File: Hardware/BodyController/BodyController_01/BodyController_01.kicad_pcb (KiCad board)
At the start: 4 copper layers, 155 x 106 mm, 402 parts, among them J1 7796, J10 Conn_01x01, J11 Conn_01x01, J12 Conn_01x01, J13 Conn_01x01, J2 Conn_01x14, J3 Conn_02x10_Top_Bottom, J4 Conn_02x10_Top_Bottom, J5 7796, J6 7796, J7 CONN_01X06, J8 USB_OTG, J9 Conn_01x01, Q1 NX1029X,115, Q10 NX1029X,115, Q12 BUK9Y3R0-40E,115, Q13 BUK9Y3R0-40E,115, Q16 2N7002, Q17 Q_PMOS_GSD, Q2 NX1029X,115, Q3 2N7002, Q4 SQJ423EP-T1_GE3, Q6 NX1029X,115, Q7 NX1029X,115, Q8 2N7002, Q9 2N7002, SW1 PTS645SM43SMTR92 LFS, U1 PIC33EPxxxMU810, U10 LM2904AVQDRQ1, U11 BTS50202EKAXUMA2, U12 BTS50202EKAXUMA2, U13 BTS50202EKAXUMA2, U14 OPA320-Q1, U15 BTS716G, U16 MCP2562-H/SN, U17 TPS70950QDBVRQ1, U18 TPS70933QDBVRQ1, U19 TPS70933QDBVRQ1, U2 LM2903QDRQ1, U20 LMR140x0, U21 LM2903QDRQ1, U22 DRV8872DDARQ1, U23 tps25940-q1, U25 UCC27511A-Q1, U27 INA21x, U29 FT230X, U3 INA21x, U4 BTS716G, U5 BTS500801TMAATMA1, U6 BTS500801TMAATMA1, U7 BTS50202EKAXUMA2, U8 BTS50202EKAXUMA2, U9 BTS50202EKAXUMA2, Y1 8MHz

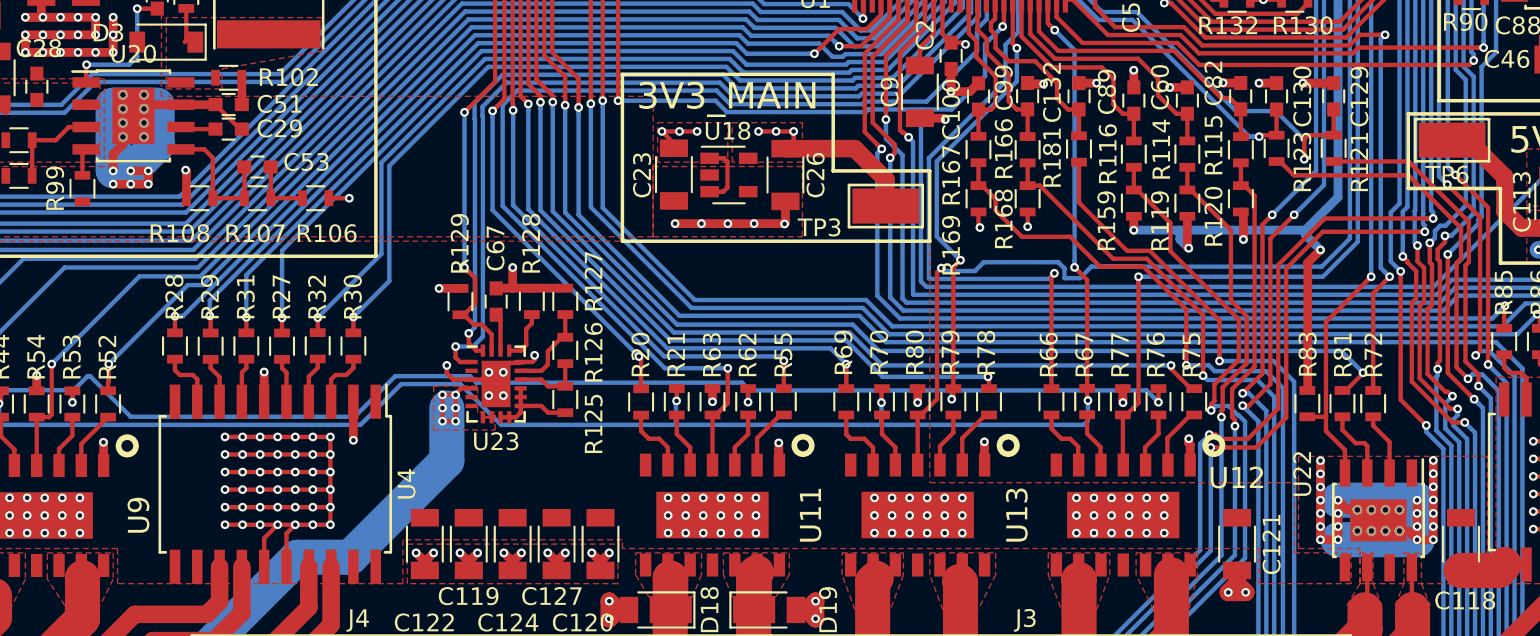
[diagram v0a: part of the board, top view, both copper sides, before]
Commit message: added BOM scripts
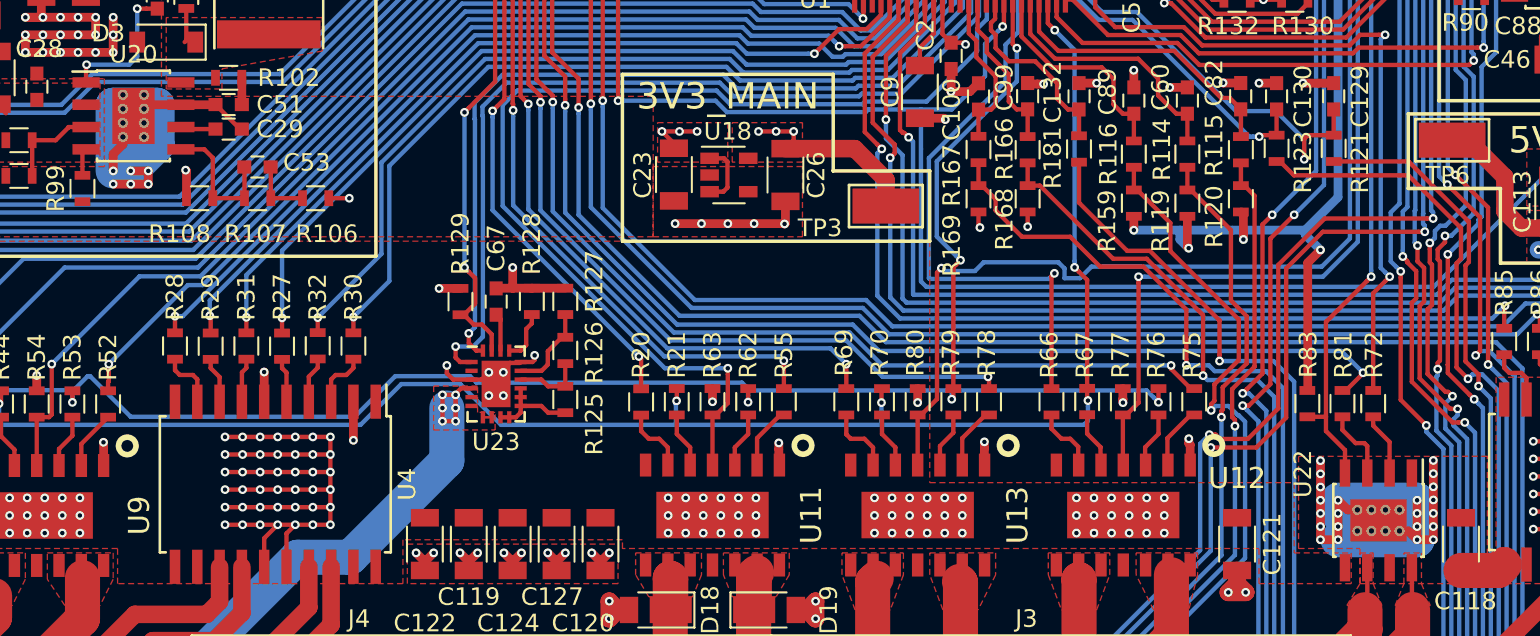
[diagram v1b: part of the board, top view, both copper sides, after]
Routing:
- net GND: track 980.4 -> 986.4 mm
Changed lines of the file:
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@@
     (thickness 1.6)
     (drawings 92)
-    (tracks 5516)
+    (tracks 5519)
     (zones 0)
     (modules 402)
@@
   (segment (start 112.5 127.752916) (end 112.499692 127.752608) (width 0.25) (layer F.Cu) (net 202))
   (segment (start 112.5 128.5) (end 112.5 127.752916) (width 0.25) (layer F.Cu) (net 202))
-  (segment (start 163.85 135.5) (end 166.25 135.5) (width 2) (layer In1.Cu) (net 209))
+  (segment (start 94.755 112.266) (end 94.355 112.266) (width 2) (layer B.Cu) (net 209))
+  (segment (start 94.355 112.266) (end 93.555 113.066) (width 2) (layer B.Cu) (net 209))
+  (segment (start 162.75 134.5) (end 167.25 134.5) (width 2) (layer B.Cu) (net 209))
   (segment (start 162.75 133.75) (end 167.25 133.75) (width 2) (layer B.Cu) (net 209))
+  (segment (start 163.85 135.5) (end 166.25 135.5) (width 2) (layer In1.Cu) (net 209))
   (segment (start 162.75 136) (end 167.25 136) (width 2) (layer B.Cu) (net 209))
   (segment (start 94.755 110.666) (end 94.755 113.066) (width 2) (layer In1.Cu) (net 209))

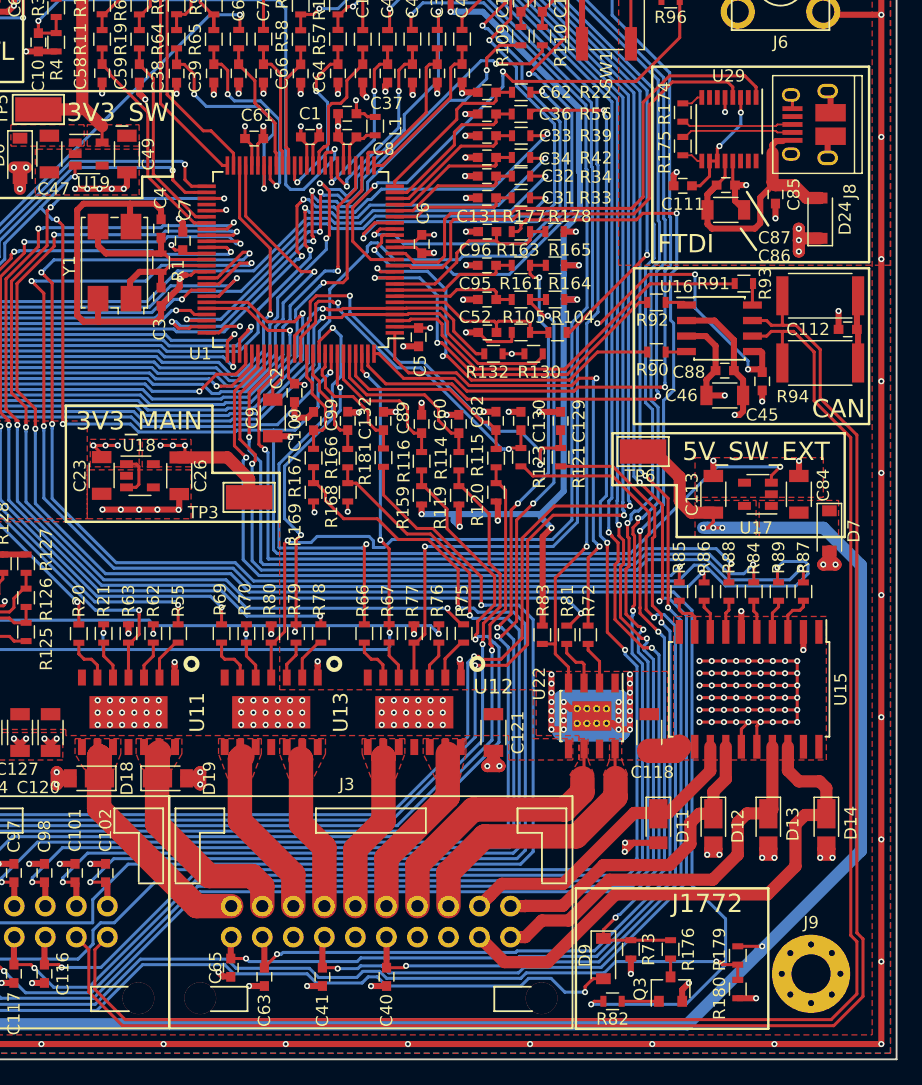
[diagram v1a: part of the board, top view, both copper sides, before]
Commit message: fixed some BOM items, changed USB to vertical mount, CAN traces thicker, J1172 sims
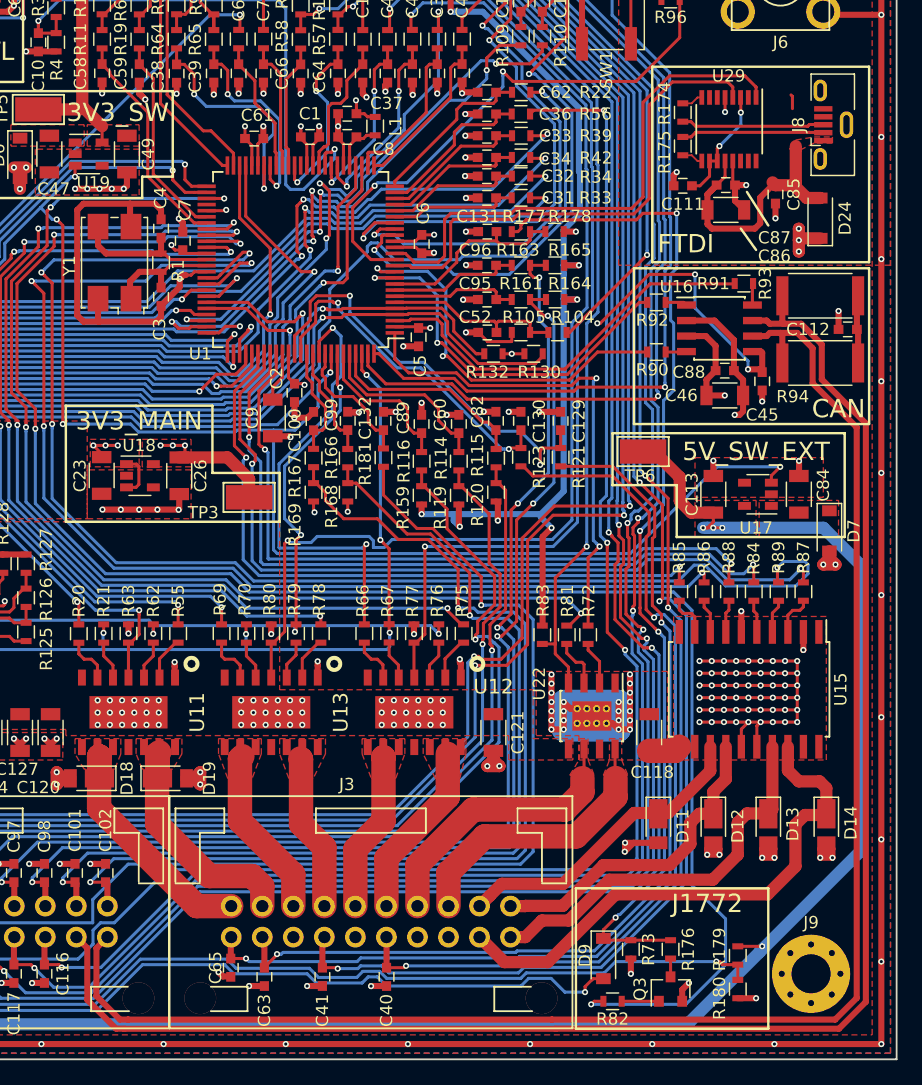
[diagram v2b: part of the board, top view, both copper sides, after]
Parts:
- J8: footprint Connectors:USB_Micro-B_10103594-0001LF -> Connectors_USB:USB_Micro-B_Vertical_Molex-105133-0001
- R176: value R -> 1k3
- R177: value R -> 340k
- R178: value R -> 100k
- R179, R180: value R -> 330R
- R181: value R -> 10k
- R73: value R -> 2k74
- R82: value R -> 100R
- moved J8 1.85 mm to (184.8, 86.5)
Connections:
- net PILOT_IN renamed PILOT
- net PROXIMITY_IN renamed PROXIMITY
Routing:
- net GND: track 986.4 -> 981.5 mm
- net USB_D+: track 9.17 -> 11.9 mm
- net USB_D-: track 9.23 -> 11.9 mm
- net USB_5V: track 24.4 -> 22.6 mm
- net CAN_P: track 133.8 -> 135.3 mm
- net (no net): track 0.00 -> 1.17 mm
- added copper zone on F.Cu, net USB_5V

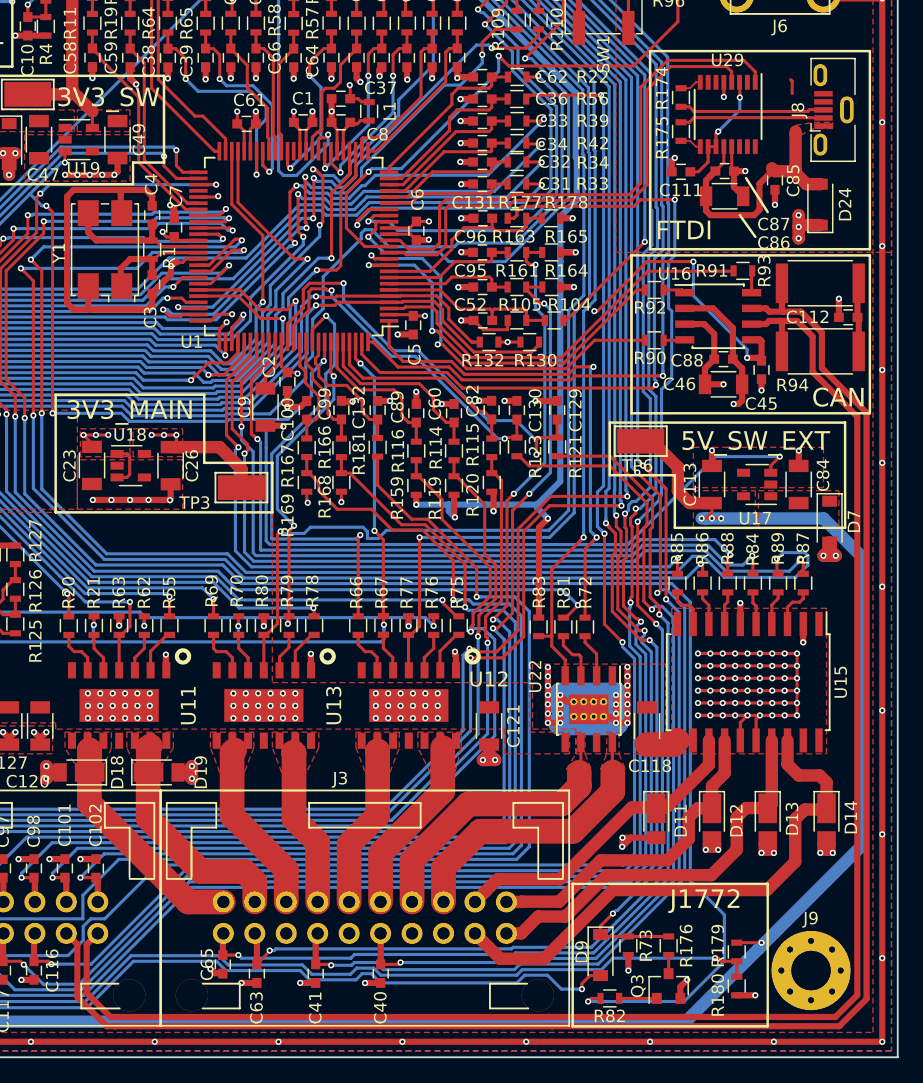
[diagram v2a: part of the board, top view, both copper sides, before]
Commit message: added CAN choke
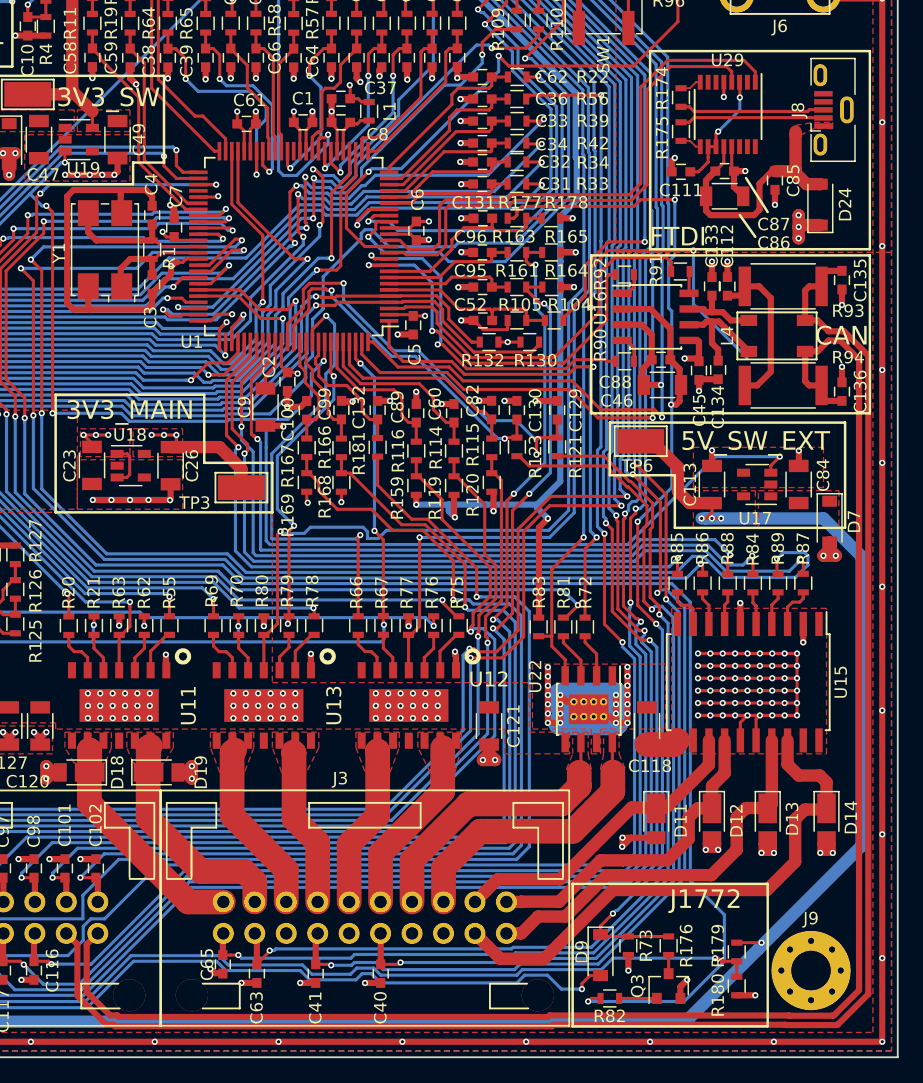
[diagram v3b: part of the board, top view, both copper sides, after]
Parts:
- added C133: 18pF, Capacitors_SMD:C_0603, F.Cu at (175.0, 100.8)
- added C134: 18pF, Capacitors_SMD:C_0603, F.Cu at (175.5, 107.5)
- added C135: 18pF, Capacitors_SMD:C_0603, F.Cu at (185.5, 100.2)
- added C136: 18pF, Capacitors_SMD:C_0603, F.Cu at (185.5, 109.2)
- added L4: EMI_Filter_CommonMode, Footprints:ACT45B, F.Cu at (180.2, 104.8)
- moved C112 10.1 mm to (176.2, 100.8), turned to 90 degrees
- moved C45 5.05 mm to (173.9, 107.5)
- moved C88 5.05 mm to (170.9, 106.7)
- moved R91 5.05 mm to (172.4, 99.5)
- moved U16 5.05 mm to (170.4, 103.2)
- moved C46 4.94 mm to (171.0, 108.7)
- moved R94 4.07 mm to (180.8, 108.8), turned to 180 degrees
- moved R93 3.01 mm to (180.8, 100.8), turned to 0 degrees
- moved R90 2.94 mm to (167.9, 106.8)
- moved R92 2.70 mm to (167.9, 99.8)
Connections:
- U16 pad 6: CAN_N -> /TopLevel/Communication/CAN_FILT_N
- U16 pad 7: CAN_P -> /TopLevel/Communication/CAN_FILT_P
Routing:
- net (no net): track 1.17 -> 22.6 mm, vias 0 -> 2
- net +3V3: track 62.3 -> 43.1 mm, vias 18 -> 16
- net /TopLevel/Communication/CAN_FILT_N: track 0.00 -> 9.30 mm
- net Net-(C112-Pad1): track 5.58 -> 13.0 mm
- net /TopLevel/Communication/CAN_FILT_P: track 0.00 -> 6.54 mm
- net GND: track 981.5 -> 986.5 mm, vias 312 -> 315
- net BATT_EN: track 178.0 -> 182.4 mm
- net DCDC_EN: track 146.5 -> 149.8 mm
- net CAN_RX: track 31.9 -> 28.9 mm
- net CAN_SLEEP: track 33.0 -> 31.1 mm
- net +12P: track 220.3 -> 221.9 mm
- net Net-(R92-Pad1): track 1.79 -> 2.47 mm
- net CAN_P: track 135.3 -> 135.9 mm
- net RADIATOR_INPUT_TEMP_OUT: track 151.6 -> 152.1 mm
- net DAC_OUT_1: track 182.4 -> 181.8 mm
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
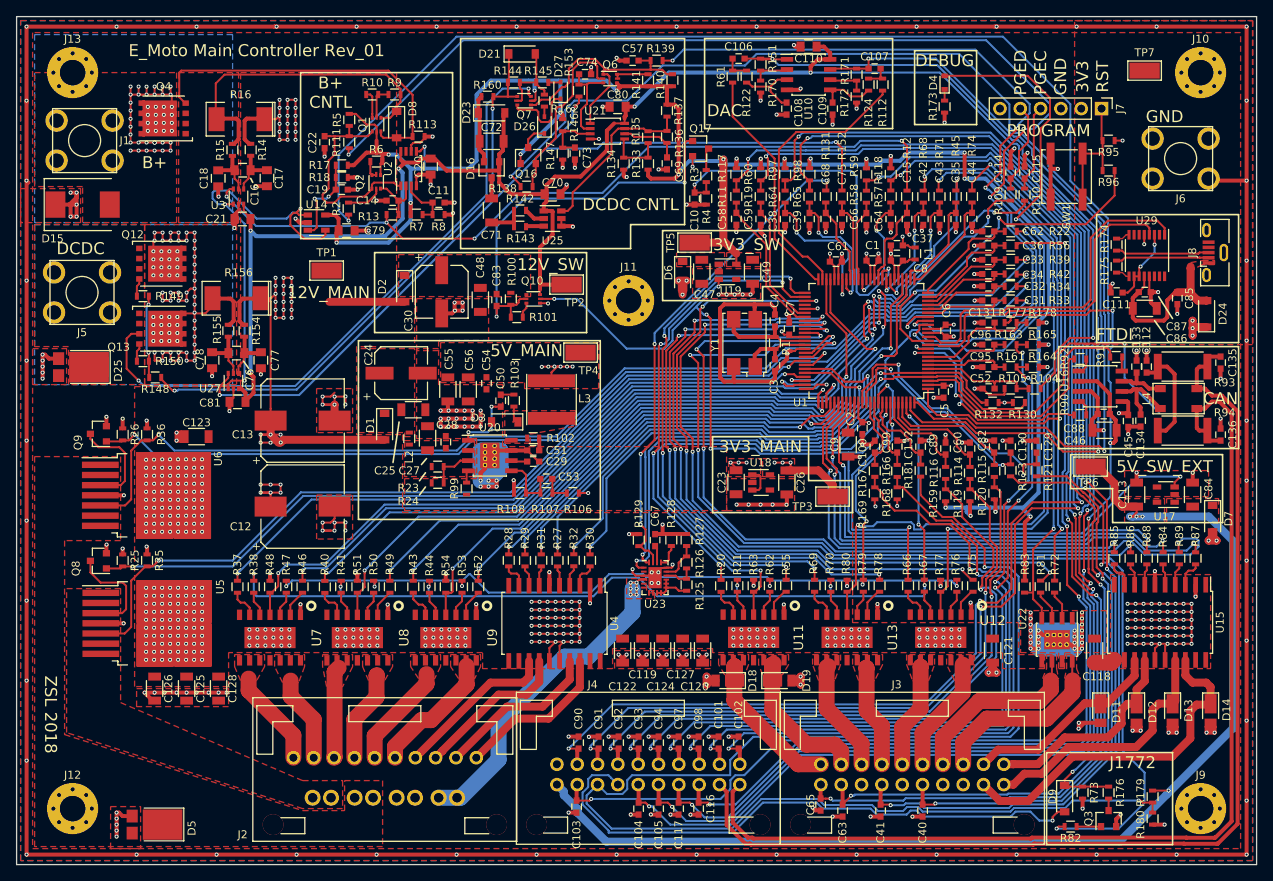
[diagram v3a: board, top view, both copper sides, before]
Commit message: Found a few DRC errors, still need to correct them
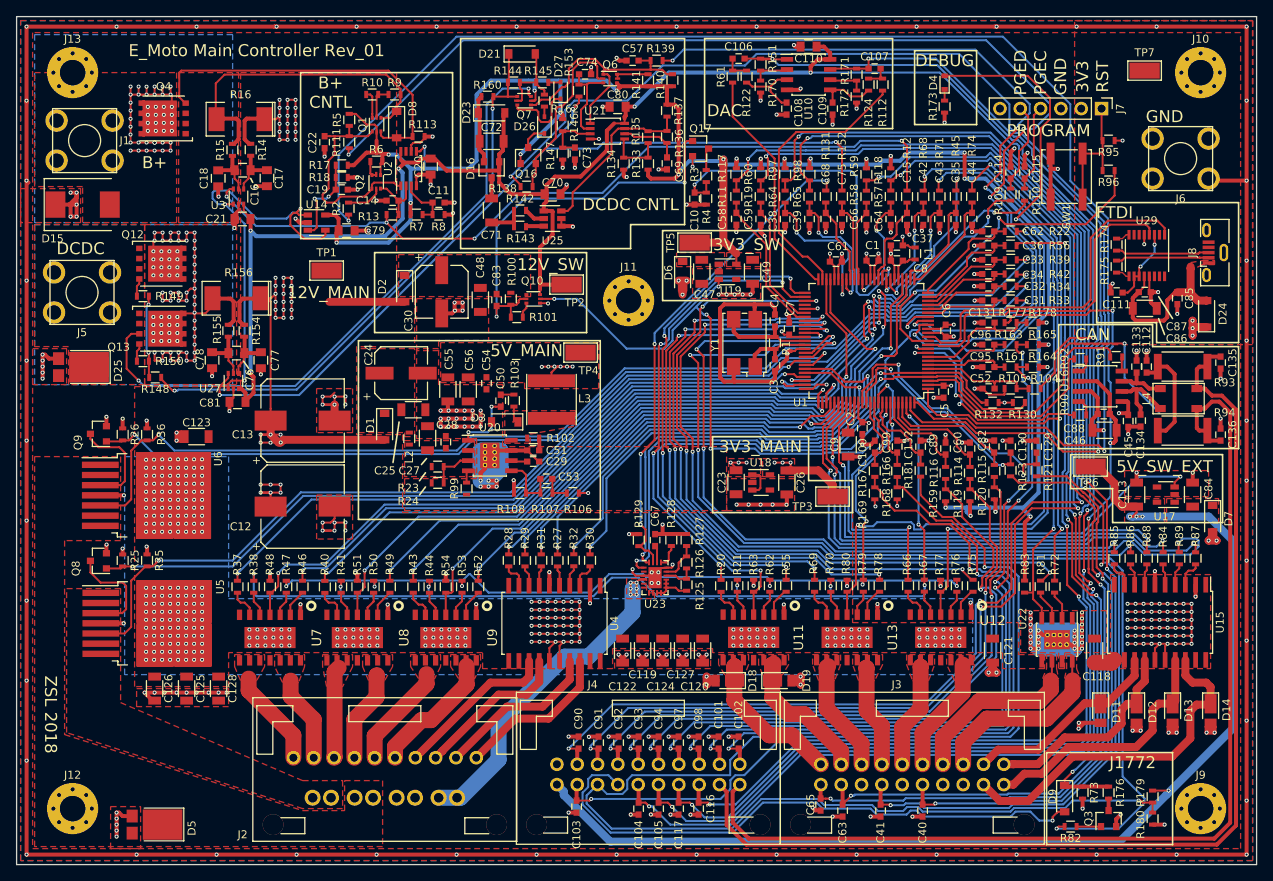
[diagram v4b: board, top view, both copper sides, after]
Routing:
- net FAN_1_OUT: track 20.3 -> 19.3 mm
- added copper zone on B.Cu, net +12V
